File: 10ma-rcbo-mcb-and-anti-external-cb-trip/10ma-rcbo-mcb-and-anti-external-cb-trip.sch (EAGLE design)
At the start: 10 parts

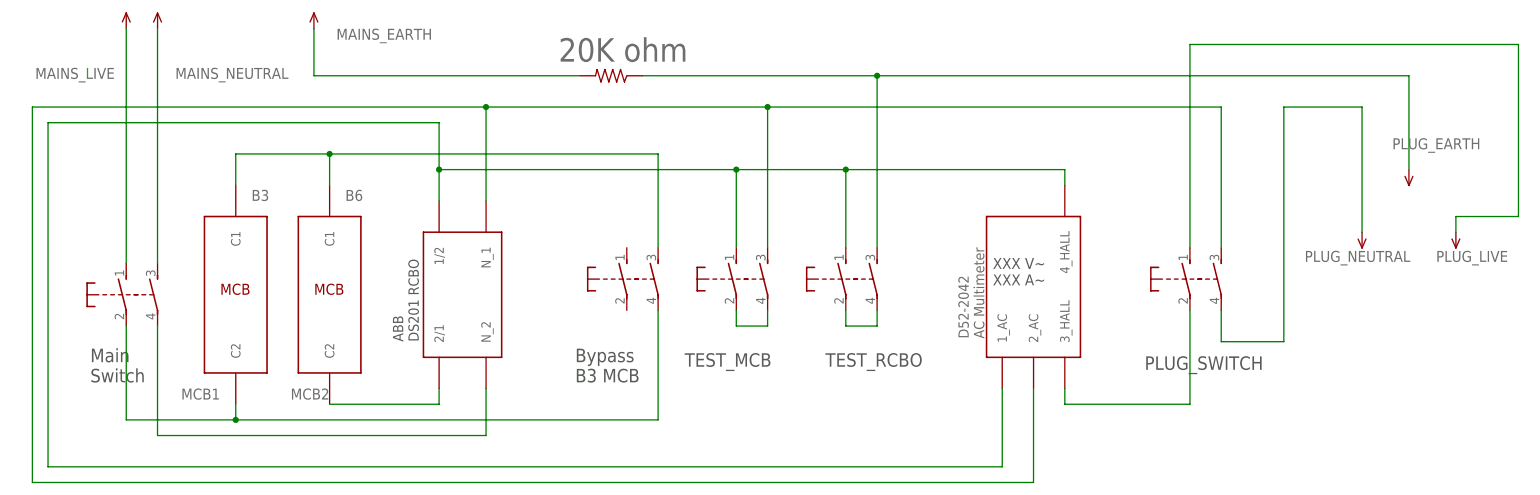
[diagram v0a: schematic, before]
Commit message: remove use of B3 MCB
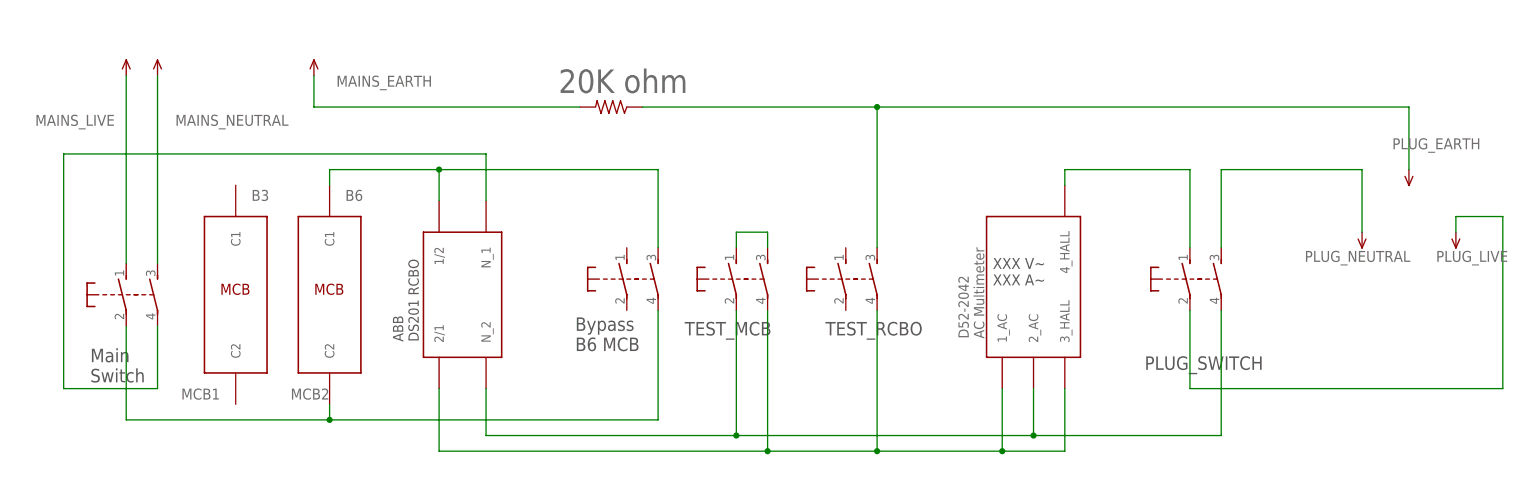
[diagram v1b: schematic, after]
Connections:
- removed net N$10: S61.P, S62.P
- removed net N$7: S12.S, S52.S, U$1.2_AC, U$2.N_1
- removed net N$8: S51.S, S61.S, U$1.1_AC, U$1.4_HALL, U$2.1/2
- new net N$2: S51.S, S52.S
- net N$1: now also MCB2.C2; no longer MCB1.C2
- net N$11: now also MCB2.C1, S42.S, U$2.1/2; no longer S11.P, U$1.3_HALL
- net N$3: now also S52.P, S62.P, U$1.1_AC, U$1.3_HALL; no longer MCB2.C2
- net N$4: now also S11.S, U$1.4_HALL; no longer S32.P, U$2.N_2
- net N$6: now also S32.P, U$2.N_1; no longer MCB1.C1, MCB2.C1, S42.S
- net N$9: now also S12.P, U$1.2_AC, U$2.N_2; no longer S52.P
- net V: now also S11.P, S12.S; no longer S11.S, S12.P
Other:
- note added: "Bypass B6 MCB"
- note removed: "Bypass B3 MCB"
